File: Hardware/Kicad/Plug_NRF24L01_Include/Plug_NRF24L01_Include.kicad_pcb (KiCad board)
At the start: 2 copper layers, 54 parts, among them J1 Conn_01x07_Socket, J2 Conn_02x07_Odd_Even, Q1 2N7002, Q2 2N7002, Q3 2N7002, Q4 2N7002, Q5 2N7002, SW1 SW_Push, U1 STM32L412KBTx, U2 MIC5219-3.3YMM, U3 nRF24L01P, Y1 16MHz

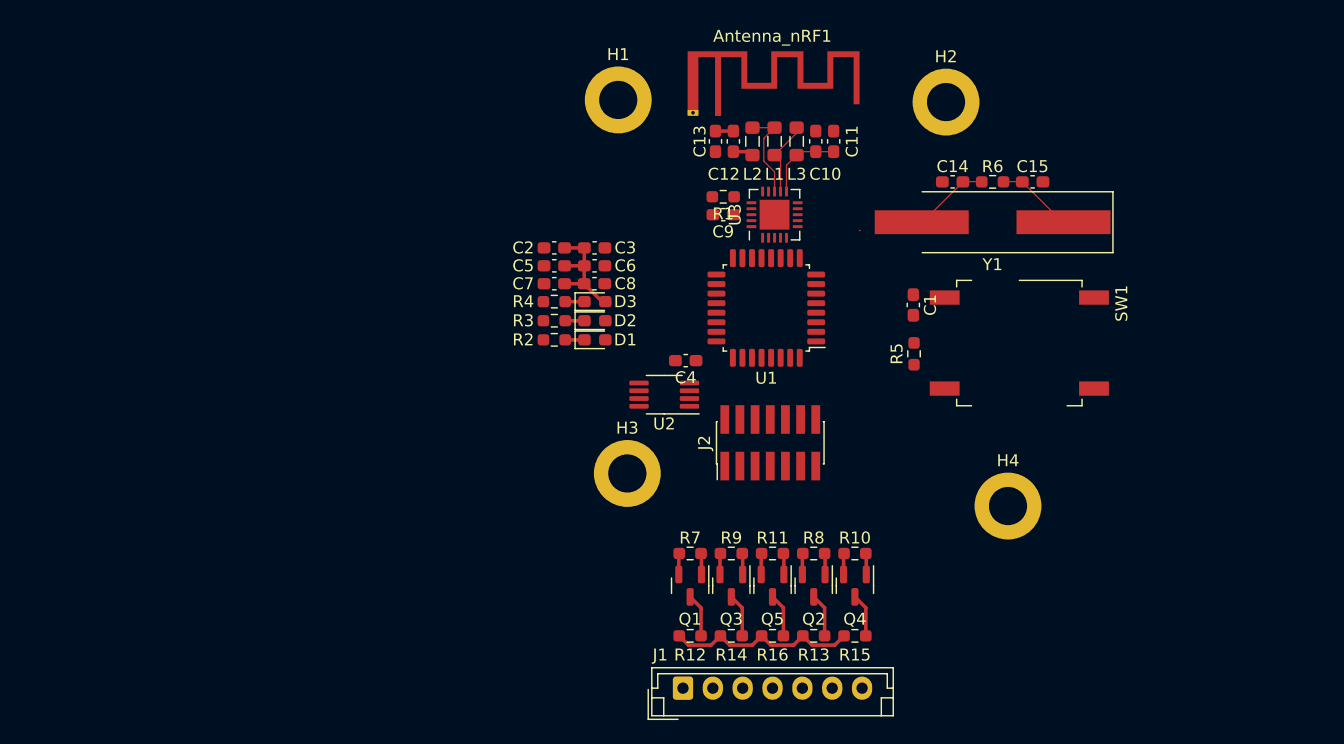
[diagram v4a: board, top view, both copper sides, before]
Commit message: Updated Plug_NRF24L01_Include. Schematic (Pins assignment / Appairing Button). PCB (Finalized routing / Antenna not working).
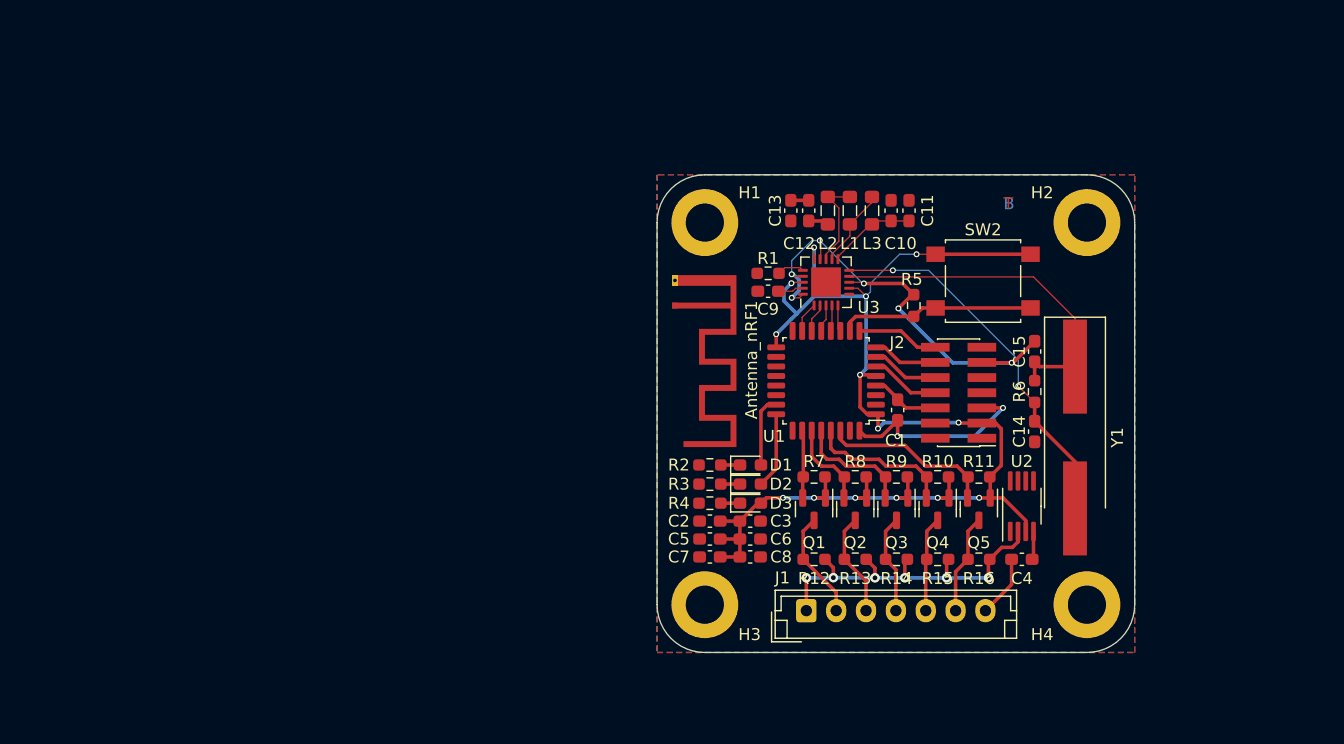
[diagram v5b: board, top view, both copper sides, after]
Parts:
- removed SW1: SW_Push, Button_Switch_SMD:SW_MEC_5GSH9
- added SW2: SW_SPST, Button_Switch_SMD:SW_SPST_B3S-1000, F.Cu at (123.3, 72.9)
- moved C4 32.7 mm to (126.5, 96.2)
- moved U2 31.4 mm to (126.5, 91.8), turned to 90 degrees
- moved C8 26.3 mm to (103.8, 96.0)
- moved C2 26.3 mm to (100.4, 93.0)
- moved C3 26.3 mm to (103.8, 93.0)
- moved C5 26.3 mm to (100.4, 94.5)
- moved C6 26.3 mm to (103.8, 94.5)
- moved C7 26.3 mm to (100.4, 96.0)
- moved C14 22.0 mm to (127.6, 85.5), turned to -90 degrees
- moved D3 21.3 mm to (103.8, 91.5)
- moved R4 21.3 mm to (100.4, 91.5)
- moved Y1 19.3 mm to (131.0, 86.0), turned to -90 degrees
- moved D2 18.9 mm to (103.8, 89.9)
- moved R3 18.9 mm to (100.4, 89.9)
- moved Q5 18.4 mm to (123.0, 92.0)
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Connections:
- C9 pad 2: GND1 -> GND
- J1 pad 7: GND3 -> GND
- J2 pad 10: unconnected-(J2-Pin_10-Pad10) -> SWDCK
- J2 pad 12: NRST -> USART2_RX
- J2 pad 13: USART2_RX -> unconnected-(J2-Pin_13-Pad13)
- J2 pad 4: SWDIO -> unconnected-(J2-Pin_4-Pad4)
- J2 pad 6: SWDCK -> NRST
- J2 pad 8: unconnected-(J2-Pin_8-Pad8) -> SWDIO
- Q1 pad 2: Serial_Data1_STM32 -> Data_Clock_STM32
- Q1 pad 3: Serial_Data1_SNES -> Data_Clock_SNES
- Q2 pad 2: Data_Clock_STM32 -> Data_Latch_STM32
- Q2 pad 3: Data_Clock_SNES -> Data_Latch_SNES
- Q3 pad 2: Data_Latch_STM32 -> Serial_Data1_STM32
- Q3 pad 3: Data_Latch_SNES -> Serial_Data1_SNES
- Q4 pad 2: IOBit_STM32 -> Serial_Data2_STM32
- Q4 pad 3: IOBit_SNES -> Serial_Data2_SNES
- Q5 pad 2: Serial_Data2_STM32 -> IOBit_STM32
- Q5 pad 3: Serial_Data2_SNES -> IOBit_SNES
- R1 pad 2: GND1 -> GND
- R10 pad 2: IOBit_STM32 -> Serial_Data2_STM32
- R11 pad 2: Serial_Data2_STM32 -> IOBit_STM32
- R12 pad 2: Serial_Data1_SNES -> Data_Clock_SNES
- R13 pad 2: Data_Clock_SNES -> Data_Latch_SNES
- R14 pad 2: Data_Latch_SNES -> Serial_Data1_SNES
- R15 pad 2: IOBit_SNES -> Serial_Data2_SNES
- R16 pad 2: Serial_Data2_SNES -> IOBit_SNES
- R7 pad 2: Serial_Data1_STM32 -> Data_Clock_STM32
- R8 pad 2: Data_Clock_STM32 -> Data_Latch_STM32
- R9 pad 2: Data_Latch_STM32 -> Serial_Data1_STM32
- U1 pad 10: SPI_Digital_Output -> Appairing_Btn
- U1 pad 11: Chip_Enable -> SPI_Digital_Output
- U1 pad 13: unconnected-(U1-PA7-Pad13) -> SPI_Clock
- U1 pad 14: unconnected-(U1-PB0-Pad14) -> SPI_Chip_Select
- U1 pad 15: unconnected-(U1-PB1-Pad15) -> Chip_Enable
- U1 pad 19: Status_LED -> unconnected-(U1-PA9-Pad19)
- U1 pad 2: Appairing_Btn -> unconnected-(U1-PC14-Pad2)
- U1 pad 20: Player1_LED -> unconnected-(U1-PA10-Pad20)
- U1 pad 23: SWDIO -> Player1_LED
- U1 pad 24: SWDCK -> Status_LED
- U1 pad 25: Serial_Data1_STM32 -> unconnected-(U1-PA15-Pad25)
- U1 pad 26: unconnected-(U1-PB3-Pad26) -> Data_Clock_STM32
- U1 pad 28: Serial_Data2_STM32 -> Serial_Data1_STM32
- U1 pad 29: Data_Clock_STM32 -> Serial_Data2_STM32
- U1 pad 6: SPI_Clock -> SWDIO
- U1 pad 7: SPI_Chip_Select -> SWDCK
- U1 pad 8: USART2_TX -> USART2_RX
- U1 pad 9: USART2_RX -> USART2_TX
- U3 pad 14: GND1 -> GND
- U3 pad 17: GND1 -> GND
- U3 pad 20: GND1 -> GND
- U3 pad 8: GND1 -> GND
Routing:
- net +3.3V: track 19.2 -> 112.6 mm, vias 0 -> 14
- net GND: track 0.00 -> 61.9 mm, vias 0 -> 8
- net XC1: track 6.43 -> 31.7 mm, vias 0 -> 2
- net XC2: track 6.43 -> 29.5 mm
- net Appairing_Btn: track 0.00 -> 16.3 mm
- net +5V: track 16.4 -> 30.4 mm, vias 0 -> 6
- net IOBit_STM32: track 1.78 -> 14.5 mm
- net Serial_Data2_STM32: track 1.78 -> 12.3 mm
- net Serial_Data1_STM32: track 1.78 -> 9.90 mm
- net USART2_TX: track 0.00 -> 6.92 mm
- net Status_LED: track 0.00 -> 6.38 mm
- net Player1_LED: track 0.00 -> 6.00 mm
- net SWDIO: track 0.00 -> 5.89 mm
- net NRST: track 0.00 -> 5.80 mm
- net SWDCK: track 0.00 -> 5.69 mm
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- added copper zone on B.Cu, net GND
- added copper zone on F.Cu, net GND
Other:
- board outline added: 40 x 40 mm
- board text added: "B"
- board text added: "T"

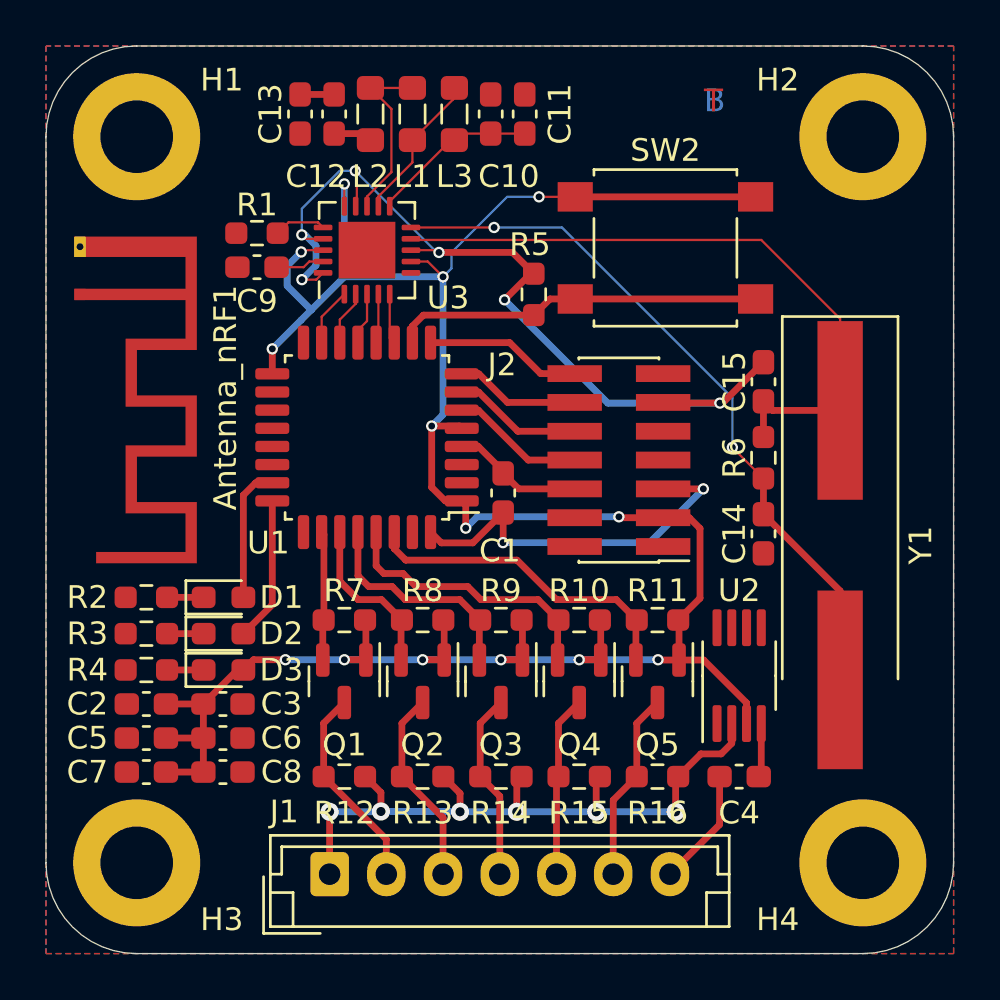
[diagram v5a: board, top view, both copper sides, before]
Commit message: Updated Plug_NRF24L01_Include (V1.1) - PCB
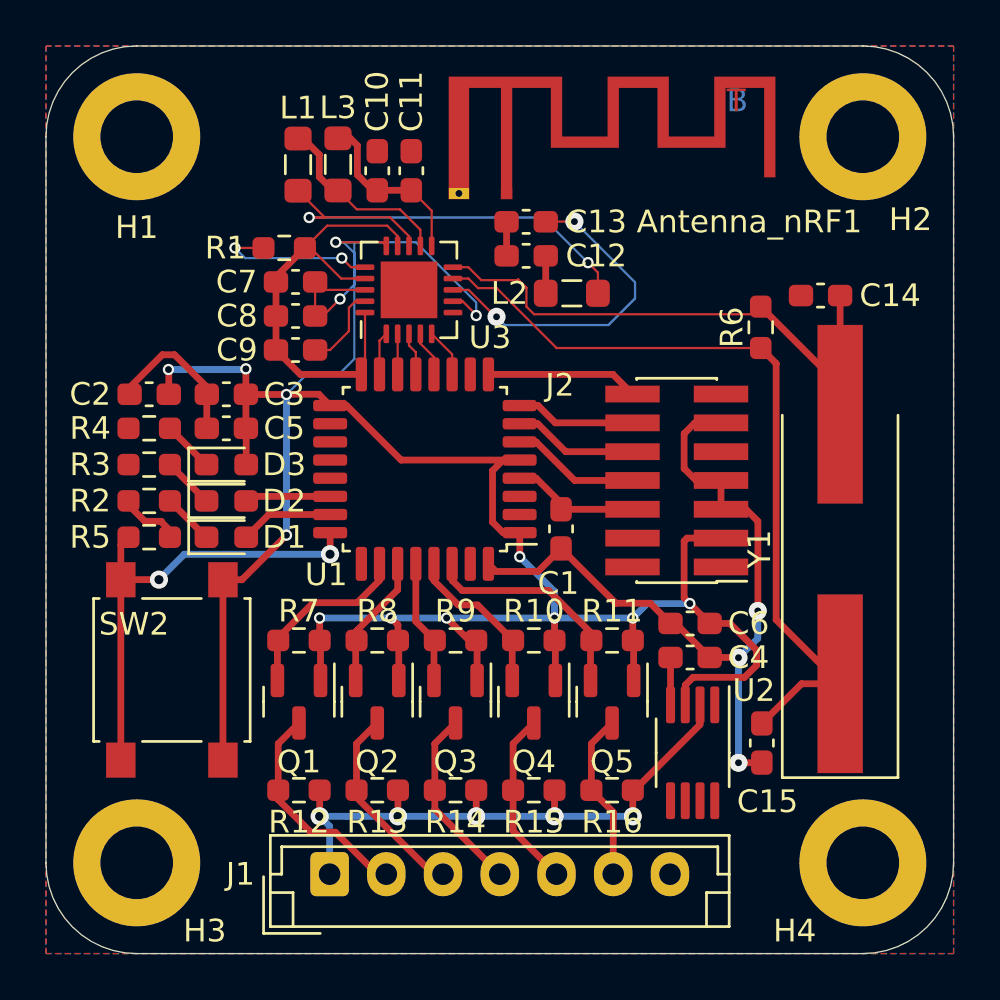
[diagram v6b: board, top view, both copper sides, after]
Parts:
- moved SW2 28.6 mm to (101.5, 91.5), turned to 90 degrees
- moved C7 22.6 mm to (107.0, 74.4)
- moved C6 21.2 mm to (124.4, 89.5), turned to 180 degrees
- moved C8 20.4 mm to (107.0, 75.9), turned to 180 degrees
- moved R5 20.0 mm to (100.5, 85.7), turned to 0 degrees
- moved Antenna_nRF1 19.3 mm to (116.3, 70.5), turned to 0 degrees
- moved C15 15.9 mm to (127.5, 94.7), turned to -90 degrees
- moved C5 14.1 mm to (104.0, 80.8)
- moved C3 13.7 mm to (104.0, 79.3), turned to 180 degrees
- moved C2 13.7 mm to (100.5, 79.3)
- moved L2 11.9 mm to (119.2, 74.9), turned to 180 degrees
- moved C13 11.0 mm to (117.2, 71.8), turned to 180 degrees
- moved C14 10.8 mm to (130.1, 75.0), turned to 180 degrees
- moved R4 10.7 mm to (100.5, 80.8)
- moved C12 10.5 mm to (117.2, 73.2), turned to 0 degrees
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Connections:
- U1 pad 10: Appairing_Btn -> unconnected-(U1-PA4-Pad10)
- U1 pad 22: unconnected-(U1-PA12-Pad22) -> Status_LED
- U1 pad 24: Status_LED -> Appairing_Btn
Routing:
- net GND: track 61.9 -> 78.7 mm, vias 8 -> 5
- net ANT2: track 7.84 -> 21.5 mm, vias 0 -> 2
- net +3.3V: track 112.6 -> 122.6 mm
- net XC2: track 29.5 -> 35.3 mm
- net Serial_Data2_STM32: track 12.3 -> 7.10 mm
- net XC1: track 31.7 -> 26.5 mm, vias 2 -> 0
- net Net-(U3-IREF): track 2.29 -> 7.34 mm, vias 0 -> 2
- net IOBit_STM32: track 14.5 -> 9.93 mm
- net Serial_Data1_STM32: track 9.90 -> 5.50 mm
- net Appairing_Btn: track 16.3 -> 20.6 mm, vias 0 -> 2
- net +5V: track 30.4 -> 27.3 mm, vias 6 -> 5
- net Status_LED: track 6.38 -> 3.78 mm
- net Data_Clock_STM32: track 5.70 -> 8.08 mm
- net Player1_LED: track 6.00 -> 4.11 mm
- net ANT1: track 6.58 -> 8.34 mm
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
